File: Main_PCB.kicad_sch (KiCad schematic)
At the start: 57 parts, among them IC1 TCN75AVUA713-VAO, IC2 24AA64T-I_OT, J1 Conn_Coaxial, J2 Conn_02x03_Odd_Even, J3 USB_C_Receptacle_USB2.0, J4 Conn_01x03_Male, J5 Conn_01x08, J6 Conn_01x08, SW1 SW_Push, SW2 SW_Push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

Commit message: made drc complete
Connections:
- net GND: now also U6.29 (GND)
- net Reset: now also U6.28 (NRST)
- net TempAlert: now reaches U6.9 (PB1)
- net TempAlert: now also IC1.3 (ALERT), U4.10 (PC2)
- no-connect marks 5 -> 12
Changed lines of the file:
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@@
   (junction (at 213.36 72.39) (diameter 0.9144) (color 0 0 0 0))
   (junction (at 342.9 237.49) (diameter 0) (color 0 0 0 0))
-  (no_connect (at 39.37 106.68))
   (no_connect (at 69.85 214.63))
   (no_connect (at 77.47 214.63))
   (no_connect (at 173.99 262.89))
   (no_connect (at 173.99 265.43))
+  (no_connect (at 359.41 57.15))
+  (no_connect (at 359.41 59.69))
+  (no_connect (at 359.41 67.31))
+  (no_connect (at 379.73 34.29))
+  (no_connect (at 379.73 41.91))
+  (no_connect (at 379.73 44.45))
+  (no_connect (at 379.73 49.53))
+  (no_connect (at 379.73 64.77))
   (wire (pts (xy 20.32 198.12) (xy 20.32 200.66))
     (stroke (width 0) (type default) (color 0 0 0 0))
@@
     (stroke (width 0) (type default) (color 0 0 0 0))
   )
+  (wire (pts (xy 396.24 36.83) (xy 379.73 36.83))
+    (stroke (width 0) (type default) (color 0 0 0 0))
+  )
   (polyline (pts (xy 13.97 15.24) (xy 13.97 62.23))
     (stroke (width 0) (type default) (color 0 0 0 0))
@@
     (effects (font (size 1.27 1.27)) (justify right bottom))
   )
+  (label "TempAlert" (at 39.37 106.68 180)
+    (effects (font (size 1.27 1.27)) (justify right bottom))
+  )
   (label "IC2_MoistureSensor_SCL1" (at 40.64 74.93 180)
     (effects (font (size 1.27 1.27)) (justify right bottom))
@@
     (effects (font (size 1.27 1.27)) (justify right bottom))
   )
+  (label "TempAlert" (at 177.8 125.73 180)
+    (effects (font (size 1.27 1.27)) (justify right bottom))
+  )
   (label "OSC32_IN" (at 187.96 156.21 180)
     (effects (font (size 1.27 1.27)) (justify right bottom))
@@
     (effects (font (size 1.27 1.27)) (justify right bottom))
   )
+  (label "TempAlert" (at 359.41 54.61 180)
+    (effects (font (size 1.27 1.27)) (justify right bottom))
+  )
   (label "D9" (at 359.41 62.23 180)
     (effects (font (size 1.27 1.27)) (justify right bottom))
@@
     (effects (font (size 1.27 1.27)) (justify right bottom))
   )
+  (label "Reset" (at 379.73 39.37 0)
+    (effects (font (size 1.27 1.27)) (justify left bottom))
+  )
   (label "IC2_MoistureSensor_SCL1" (at 379.73 46.99 0)
     (effects (font (size 1.27 1.27)) (justify left bottom))
@@
     (pin "1")
   )
+  (symbol (lib_id "power:GND") (at 396.24 36.83 90) (unit 1)
+    (in_bom yes) (on_board yes)
+    (property "Reference" "#PWR?" (id 0) (at 402.59 36.83 0)
+      (effects (font (size 1.27 1.27)) hide)
+    )
+    (property "Value" "GND" (id 1) (at 400.05 39.3701 0)
+      (effects (font (size 1.27 1.27)) (justify left))
+    )
+    (property "Footprint" "" (id 2) (at 396.24 36.83 0)
+      (effects (font (size 1.27 1.27)) hide)
+    )
+    (property "Datasheet" "" (id 3) (at 396.24 36.83 0)
+      (effects (font (size 1.27 1.27)) hide)
+    )
+    (pin "1")
+  )
   (symbol (lib_id "Device:Fuse") (at 20.32 204.47 0) (unit 1)
     (in_bom yes) (on_board yes) (fields_autoplaced)
@@
       (reference "#PWR0174") (unit 1) (value "VCC") (footprint "")
     )
+    (path "/985c80f7-99d2-495d-8672-e26159befa43"
+      (reference "#PWR?") (unit 1) (value "GND") (footprint "")
+    )
     (path "/f1661ef2-877d-45ff-a032-83d09dbdea8d"

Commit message: updated eeprom footprint
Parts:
- removed IC2: 24AA64T-I_OT, 24AA64T-I_OT:SOT95P270X145-5N, symbol 24AA64T-I_OT:24AA64T-I_OT
- added R14: 0R, Resistor_SMD:R_0603_1608Metric_Pad0.98x0.95mm_HandSolder, symbol Device:R
- added U8: 24LC64-I/SN, 24LC64-I_SN:SOIC127P599X175-8N, symbol 24LC64-I_SN:24LC64-I/SN
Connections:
- net GND: now also R14.2, U8.1 (A0), U8.2 (A1), U8.3 (A2), U8.4 (VSS)
- net IC2_MoistureSensor_SCL1: now also U8.6 (SCL)
- net IC2_MoistureSensor_SDA1: now also U8.5 (SDA)
- net VCC: now also U8.8 (VCC)
- new net: R14.1, U8.7 (WP)
- no-connect marks 12 -> 45
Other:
- note added: "board-wire-board connectors"
- note added: "main microcontroller"
- note added: "nucleo-32 headers"
- company: (none) -> Pulu
- title: (none) -> Pulu soil monitor v1.0
- moved on the sheet: C1, C10, C11, C12, C14, C15, C16, C17, C18, C19, C2, C20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

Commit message: separated pcb desgin into two
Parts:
- U8: footprint 24LC64-I_SN:SOIC127P599X175-8N -> Package_SO:SOIC-8_3.9x4.9mm_P1.27mm
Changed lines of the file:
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@@
   (junction (at 35.56 40.64) (diameter 0) (color 0 0 0 0))
   (junction (at 45.72 77.47) (diameter 0) (color 0 0 0 0))
-  (junction (at 45.72 80.01) (diameter 0) (color 0 0 0 0))
   (junction (at 45.72 220.98) (diameter 0) (color 0 0 0 0))
   (junction (at 57.15 50.8) (diameter 0) (color 0 0 0 0))
@@
   )
   (symbol (lib_id "24LC64-I_SN:24LC64-I/SN") (at 63.5 82.55 0) (unit 1)
-    (in_bom yes) (on_board yes)
-    (property "Reference" "U8" (id 0) (at 48.26 68.58 0))
-    (property "Value" "24LC64-I/SN" (id 1) (at 44.45 66.04 0))
-    (property "Footprint" "24LC64-I_SN:SOIC127P599X175-8N" (id 2) (at 63.5 82.55 0)
+    (in_bom yes) (on_board yes) (fields_autoplaced)
+    (property "Reference" "U8" (id 0) (at 63.5 62.23 0))
+    (property "Value" "24LC64-I/SN" (id 1) (at 63.5 64.77 0))
+    (property "Footprint" "Package_SO:SOIC-8_3.9x4.9mm_P1.27mm" (id 2) (at 63.5 82.55 0)
       (effects (font (size 1.27 1.27)) (justify left bottom) hide)
     )
@@
       (reference "U7") (unit 1) (value "USBLC6-2SC6") (footprint "Package_TO_SOT_SMD:SOT-23-6")
     )
-    (path "/f9b7971d-31bb-4876-ba5e-95f8decdecc8"
-      (reference "U8") (unit 1) (value "24LC64-I/SN") (footprint "24LC64-I_SN:SOIC127P599X175-8N")
+    (path "/473e6e3f-390a-4960-8924-5cf2a70e75e8"
+      (reference "U8") (unit 1) (value "24LC64-I/SN") (footprint "Package_SO:SOIC-8_3.9x4.9mm_P1.27mm")
     )
     (path "/00e27d5e-3569-407a-bbbc-d1bff05d0d8d"

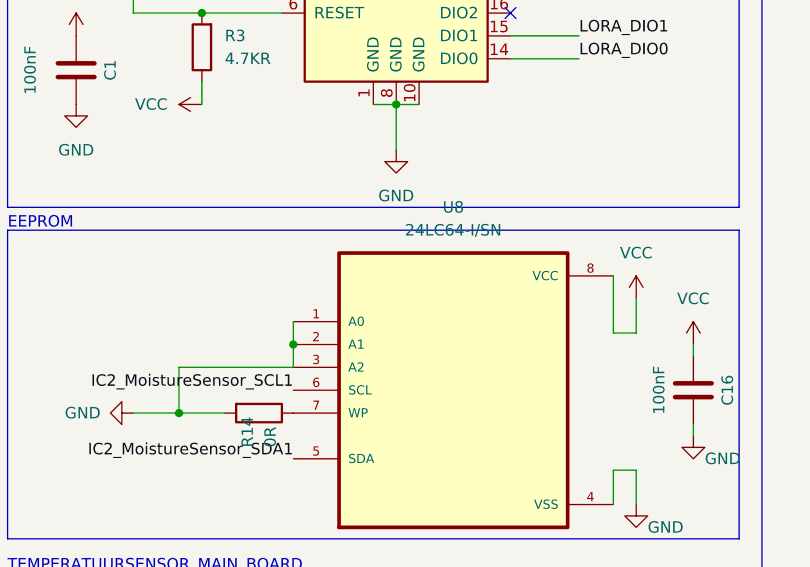
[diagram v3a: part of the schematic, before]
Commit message: added battery 3d model and exported to blender for rendering
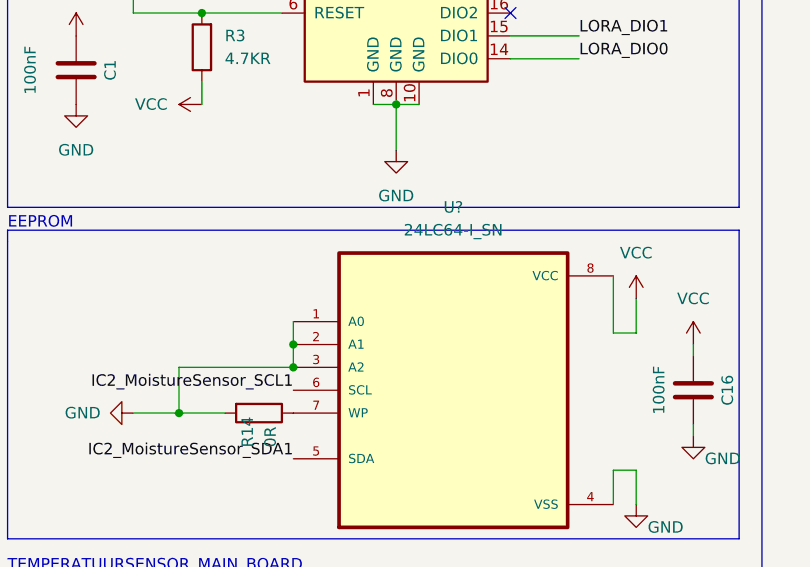
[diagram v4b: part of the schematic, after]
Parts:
- removed U8: 24LC64-I/SN, Package_SO:SOIC-8_3.9x4.9mm_P1.27mm, symbol 24LC64-I_SN:24LC64-I/SN
- added U?: 24LC64-I_SN, Package_SO:SOP-8_3.9x4.9mm_P1.27mm, symbol 24LC64_I_SN:24LC64-I_SN
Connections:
- net GND: now also U?.1 (A0), U?.2 (A1), U?.3 (A2), U?.4 (VSS)
- net IC2_MoistureSensor_SCL1: now also U?.6 (SCL)
- net IC2_MoistureSensor_SDA1: now also U?.5 (SDA)
- net VCC: now also U?.8 (VCC)
- net at R14.1: now also U?.7 (WP)
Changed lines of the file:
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@@
   (junction (at 35.56 40.64) (diameter 0) (color 0 0 0 0))
   (junction (at 45.72 77.47) (diameter 0) (color 0 0 0 0))
+  (junction (at 45.72 80.01) (diameter 0) (color 0 0 0 0))
   (junction (at 45.72 220.98) (diameter 0) (color 0 0 0 0))
   (junction (at 57.15 50.8) (diameter 0) (color 0 0 0 0))
@@
     (pin "S1")
   )
-  (symbol (lib_id "24LC64-I_SN:24LC64-I/SN") (at 63.5 82.55 0) (unit 1)
+  (symbol (lib_id "24LC64_I_SN:24LC64-I_SN") (at 63.5 82.55 0) (unit 1)
     (in_bom yes) (on_board yes) (fields_autoplaced)
-    (property "Reference" "U8" (id 0) (at 63.5 62.23 0))
-    (property "Value" "24LC64-I/SN" (id 1) (at 63.5 64.77 0))
-    (property "Footprint" "Package_SO:SOIC-8_3.9x4.9mm_P1.27mm" (id 2) (at 63.5 82.55 0)
+    (property "Reference" "U?" (id 0) (at 63.5 62.23 0))
+    (property "Value" "24LC64-I_SN" (id 1) (at 63.5 64.77 0))
+    (property "Footprint" "Package_SO:SOP-8_3.9x4.9mm_P1.27mm" (id 2) (at 63.5 82.55 0)
       (effects (font (size 1.27 1.27)) (justify left bottom) hide)
     )
@@
       (reference "U7") (unit 1) (value "USBLC6-2SC6") (footprint "Package_TO_SOT_SMD:SOT-23-6")
     )
-    (path "/473e6e3f-390a-4960-8924-5cf2a70e75e8"
-      (reference "U8") (unit 1) (value "24LC64-I/SN") (footprint "Package_SO:SOIC-8_3.9x4.9mm_P1.27mm")
+    (path "/dce7b82a-3310-42ae-808f-45cebe1d0d0d"
+      (reference "U?") (unit 1) (value "24LC64-I_SN") (footprint "Package_SO:SOP-8_3.9x4.9mm_P1.27mm")
     )
     (path "/00e27d5e-3569-407a-bbbc-d1bff05d0d8d"

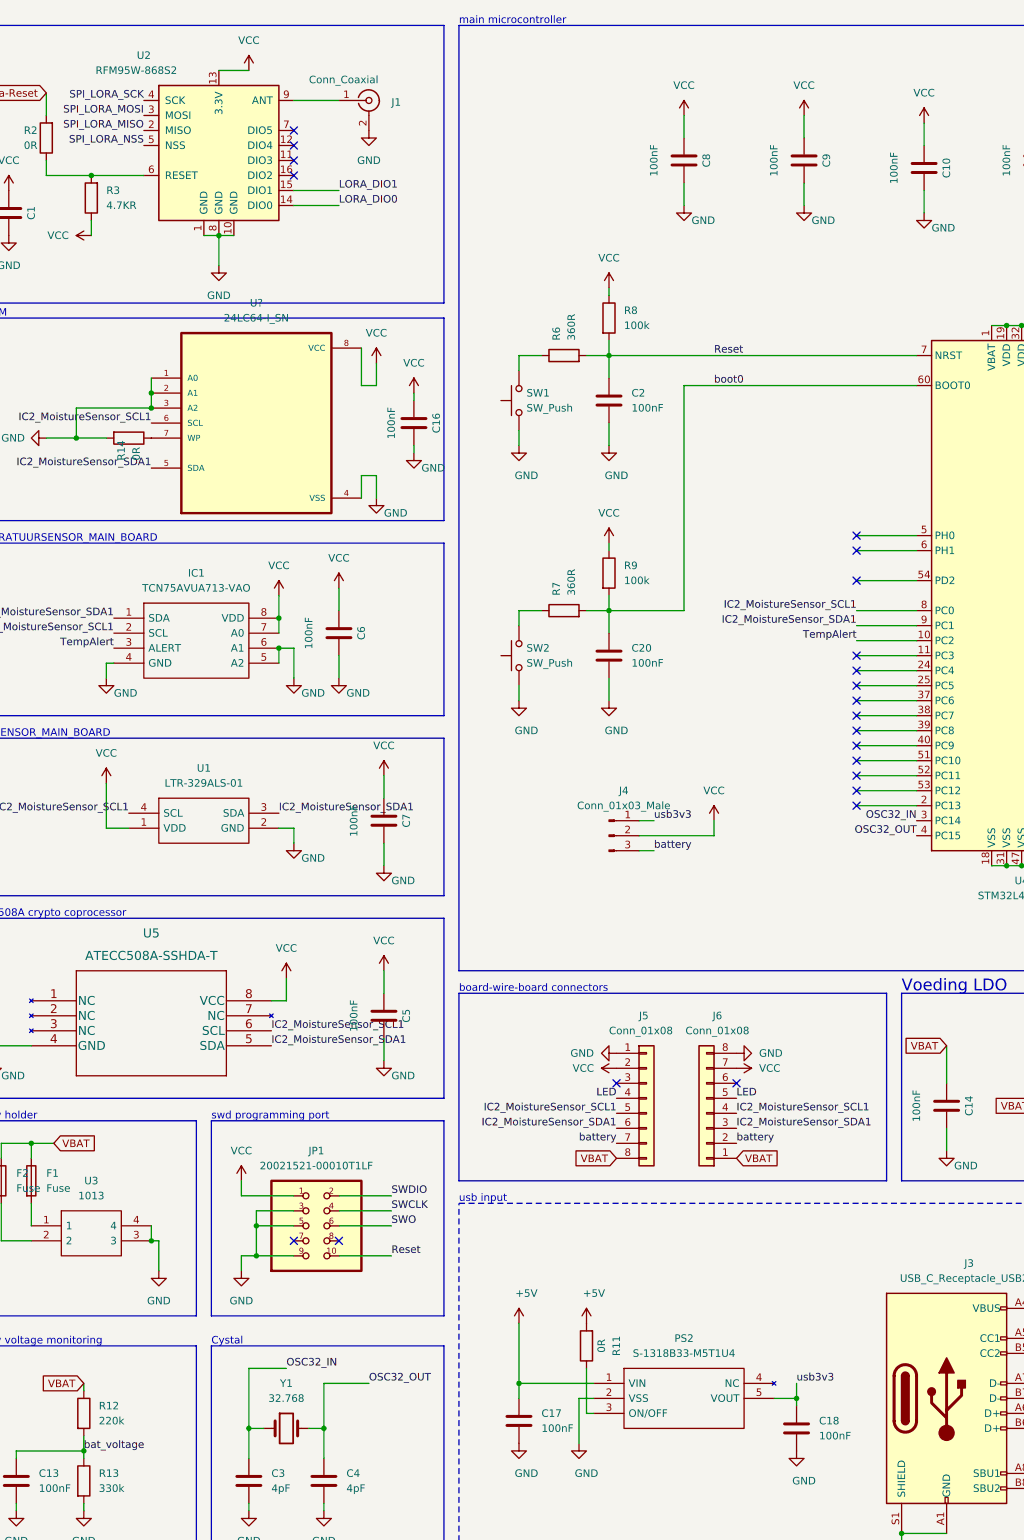
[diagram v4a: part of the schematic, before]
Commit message: made pcb order ready and ordered on jlcpcb
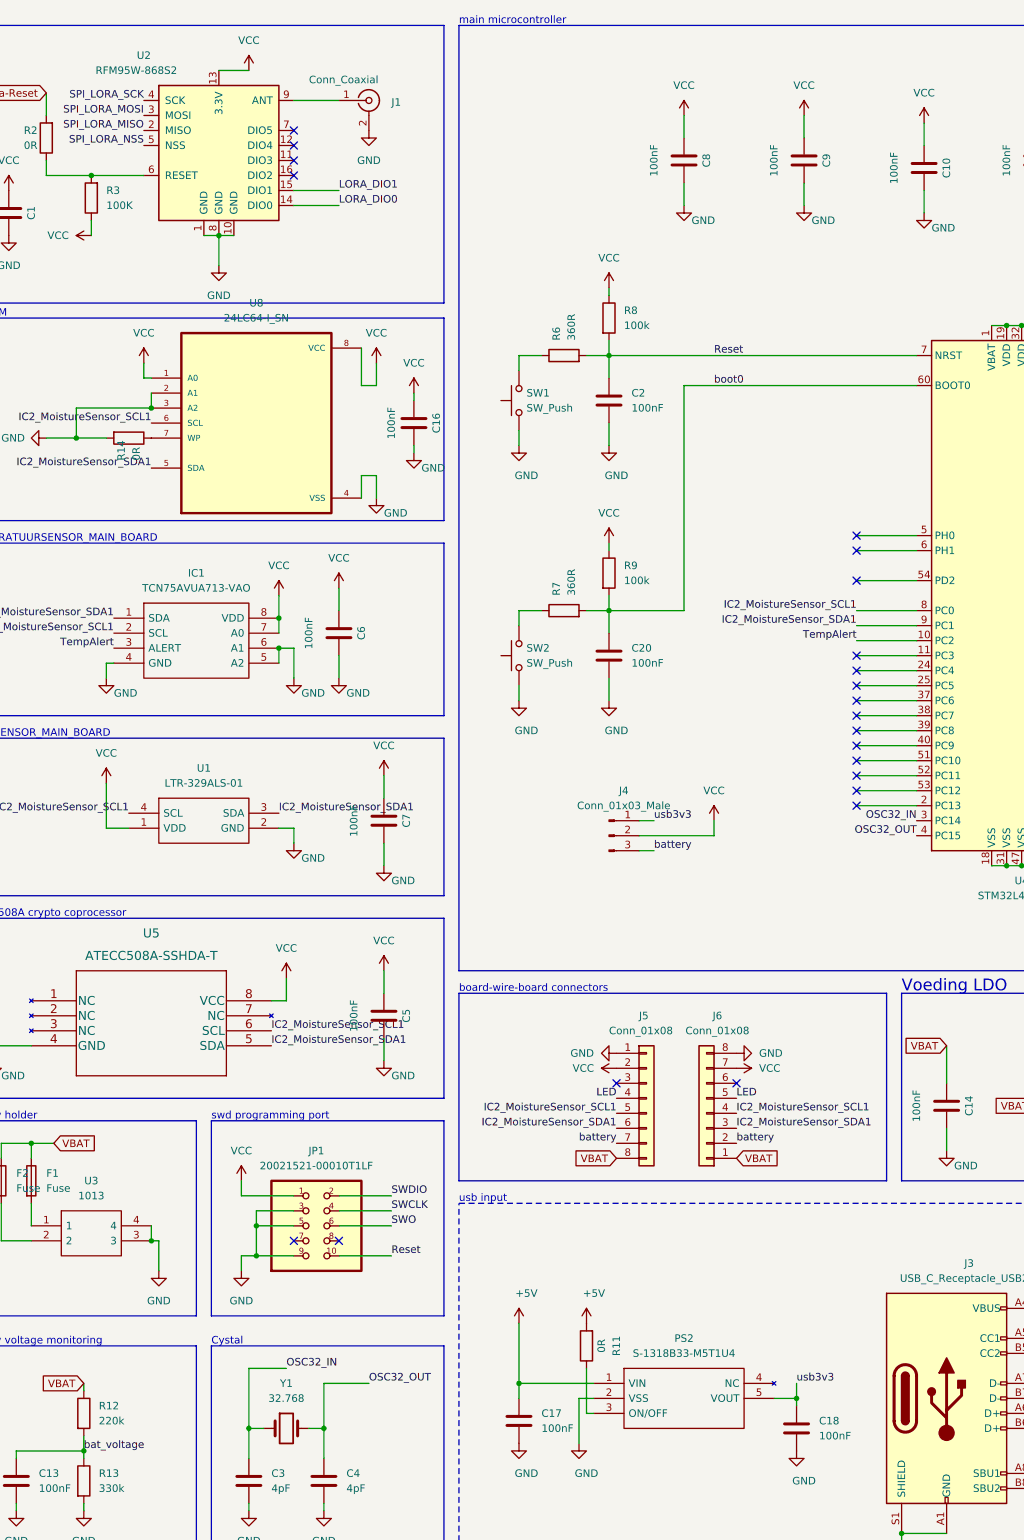
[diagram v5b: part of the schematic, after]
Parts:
- R3: value 4.7KR -> 100K
- gave numbers to parts that had none: 1
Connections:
- net GND: no longer U8.1 (A0)
- net VCC: now also U8.1 (A0)
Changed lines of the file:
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@@
   (junction (at 34.29 256.54) (diameter 0) (color 0 0 0 0))
   (junction (at 35.56 40.64) (diameter 0) (color 0 0 0 0))
-  (junction (at 45.72 77.47) (diameter 0) (color 0 0 0 0))
   (junction (at 45.72 80.01) (diameter 0) (color 0 0 0 0))
   (junction (at 45.72 220.98) (diameter 0) (color 0 0 0 0))
@@
     (stroke (width 0) (type default) (color 0 0 0 0))
   )
-  (wire (pts (xy 45.72 74.93) (xy 45.72 77.47))
+  (wire (pts (xy 44.45 74.93) (xy 44.45 72.39))
+    (stroke (width 0) (type default) (color 0 0 0 0))
+  )
+  (wire (pts (xy 45.72 74.93) (xy 44.45 74.93))
     (stroke (width 0) (type default) (color 0 0 0 0))
   )
@@
     (pin "1")
   )
+  (symbol (lib_id "power:VCC") (at 44.45 72.39 0) (unit 1)
+    (in_bom yes) (on_board yes) (fields_autoplaced)
+    (property "Reference" "#PWR?" (id 0) (at 44.45 76.2 0)
+      (effects (font (size 1.27 1.27)) hide)
+    )
+    (property "Value" "VCC" (id 1) (at 44.45 67.31 0))
+    (property "Footprint" "" (id 2) (at 44.45 72.39 0)
+      (effects (font (size 1.27 1.27)) hide)
+    )
+    (property "Datasheet" "" (id 3) (at 44.45 72.39 0)
+      (effects (font (size 1.27 1.27)) hide)
+    )
+    (pin "1")
+  )
   (symbol (lib_id "power:VCC") (at 60.96 210.82 0) (unit 1)
     (in_bom yes) (on_board yes) (fields_autoplaced)
@@
       (effects (font (size 1.27 1.27)) (justify right))
     )
-    (property "Value" "4.7KR" (id 1) (at 38.1 45.7199 0)
+    (property "Value" "100K" (id 1) (at 38.1 45.7199 0)
       (effects (font (size 1.27 1.27)) (justify right))
     )
@@
   (symbol (lib_id "24LC64_I_SN:24LC64-I_SN") (at 63.5 82.55 0) (unit 1)
     (in_bom yes) (on_board yes) (fields_autoplaced)
-    (property "Reference" "U?" (id 0) (at 63.5 62.23 0))
+    (property "Reference" "U8" (id 0) (at 63.5 62.23 0))
     (property "Value" "24LC64-I_SN" (id 1) (at 63.5 64.77 0))
     (property "Footprint" "Package_SO:SOP-8_3.9x4.9mm_P1.27mm" (id 2) (at 63.5 82.55 0)
@@
       (reference "#PWR0175") (unit 1) (value "GND") (footprint "")
     )
+    (path "/97cde102-d0df-4e47-ab29-074cec92fd01"
+      (reference "#PWR?") (unit 1) (value "VCC") (footprint "")
+    )
     (path "/f1661ef2-877d-45ff-a032-83d09dbdea8d"
       (reference "C1") (unit 1) (value "100nF") (footprint "Capacitor_SMD:C_0603_1608Metric_Pad1.08x0.95mm_HandSolder")
@@
     )
     (path "/9008efce-5f35-488d-8461-7ed8deb3fb7d"
-      (reference "R3") (unit 1) (value "4.7KR") (footprint "Resistor_SMD:R_0603_1608Metric_Pad0.98x0.95mm_HandSolder")
+      (reference "R3") (unit 1) (value "100K") (footprint "Resistor_SMD:R_0603_1608Metric_Pad0.98x0.95mm_HandSolder")
     )
     (path "/87514acd-4cbc-4e48-b356-3b42cd287830"
@@
     )
     (path "/dce7b82a-3310-42ae-808f-45cebe1d0d0d"
-      (reference "U?") (unit 1) (value "24LC64-I_SN") (footprint "Package_SO:SOP-8_3.9x4.9mm_P1.27mm")
+      (reference "U8") (unit 1) (value "24LC64-I_SN") (footprint "Package_SO:SOP-8_3.9x4.9mm_P1.27mm")
     )
     (path "/00e27d5e-3569-407a-bbbc-d1bff05d0d8d"
